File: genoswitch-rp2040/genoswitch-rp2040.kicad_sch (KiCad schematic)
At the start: 35 parts, among them J1 USB_B_Micro, J2 Conn_01x03_Socket-PicoDebug, SW1 BOOTSEL, U1 NCP1117-3.3_SOT223, U2 W25Q128JVS, U3 RP2040, U4 MCP1501-10xCH, U5_HW-SPI0 MCP3008, U6_HW-SPI1 MCP3008, U7_PIO-SPI0 MCP3008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

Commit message: Add 0201/0603M footprints for resistors, capacitors
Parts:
- C1, C10, C101, C11, C12, C13, C14, C15, C16, C4, C5, C6, C7, C8, C9: footprint (none) -> Capacitor_SMD:C_0201_0603Metric
- R1, R2, R3, R4, R5: footprint (none) -> Resistor_SMD:R_0201_0603Metric
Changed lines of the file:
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@@
       (effects (font (size 1.27 1.27)) (justify left))
     )
-    (property "Footprint" "" (at 70.8152 31.75 0)
+    (property "Footprint" "Capacitor_SMD:C_0201_0603Metric" (at 70.8152 31.75 0)
       (effects (font (size 1.27 1.27)) hide)
     )
@@
       (effects (font (size 1.27 1.27)) (justify left))
     )
-    (property "Footprint" "" (at 168.402 25.4 90)
+    (property "Footprint" "Resistor_SMD:R_0201_0603Metric" (at 168.402 25.4 90)
       (effects (font (size 1.27 1.27)) hide)
     )
@@
       (effects (font (size 1.27 1.27)))
     )
-    (property "Footprint" "" (at 354.33 21.8948 0)
+    (property "Footprint" "Capacitor_SMD:C_0201_0603Metric" (at 354.33 21.8948 0)
       (effects (font (size 1.27 1.27)) hide)
     )
@@
       (effects (font (size 1.27 1.27)) (justify left))
     )
-    (property "Footprint" "" (at 168.402 35.56 90)
+    (property "Footprint" "Resistor_SMD:R_0201_0603Metric" (at 168.402 35.56 90)
       (effects (font (size 1.27 1.27)) hide)
     )
@@
       (effects (font (size 1.27 1.27)))
     )
-    (property "Footprint" "" (at 349.25 178.308 90)
+    (property "Footprint" "Resistor_SMD:R_0201_0603Metric" (at 349.25 178.308 90)
       (effects (font (size 1.27 1.27)) hide)
     )
@@
       (effects (font (size 1.27 1.27)) (justify left))
     )
-    (property "Footprint" "" (at 108.9152 31.75 0)
+    (property "Footprint" "Capacitor_SMD:C_0201_0603Metric" (at 108.9152 31.75 0)
       (effects (font (size 1.27 1.27)) hide)
     )
@@
       (effects (font (size 1.27 1.27)) (justify left))
     )
-    (property "Footprint" "" (at 39.0652 31.75 0)
+    (property "Footprint" "Capacitor_SMD:C_0201_0603Metric" (at 39.0652 31.75 0)
       (effects (font (size 1.27 1.27)) hide)
     )
@@
       (effects (font (size 1.27 1.27)))
     )
-    (property "Footprint" "" (at 335.28 35.052 90)
+    (property "Footprint" "Resistor_SMD:R_0201_0603Metric" (at 335.28 35.052 90)
       (effects (font (size 1.27 1.27)) hide)
     )
@@
       (effects (font (size 1.27 1.27)) (justify right))
     )
-    (property "Footprint" "" (at 190.8048 179.07 0)
+    (property "Footprint" "Capacitor_SMD:C_0201_0603Metric" (at 190.8048 179.07 0)
       (effects (font (size 1.27 1.27)) hide)
     )
@@
       (effects (font (size 1.27 1.27)) (justify left))
     )
-    (property "Footprint" "" (at 51.7652 44.45 0)
+    (property "Footprint" "Capacitor_SMD:C_0201_0603Metric" (at 51.7652 44.45 0)
       (effects (font (size 1.27 1.27)) hide)
     )
@@
       (effects (font (size 1.27 1.27)) (justify left))
     )
-    (property "Footprint" "" (at 171.1452 49.53 0)
+    (property "Footprint" "Capacitor_SMD:C_0201_0603Metric" (at 171.1452 49.53 0)
       (effects (font (size 1.27 1.27)) hide)
     )
@@
       (effects (font (size 1.27 1.27)) (justify left))
     )
-    (property "Footprint" "" (at 53.0352 31.75 0)
+    (property "Footprint" "Capacitor_SMD:C_0201_0603Metric" (at 53.0352 31.75 0)
       (effects (font (size 1.27 1.27)) hide)
     )
@@
       (effects (font (size 1.27 1.27)) (justify left))
     )
-    (property "Footprint" "" (at 398.4752 231.14 0)
+    (property "Footprint" "Capacitor_SMD:C_0201_0603Metric" (at 398.4752 231.14 0)
       (effects (font (size 1.27 1.27)) hide)
     )
@@
       (effects (font (size 1.27 1.27)) (justify left))
     )
-    (property "Footprint" "" (at 107.6452 53.34 0)
+    (property "Footprint" "Capacitor_SMD:C_0201_0603Metric" (at 107.6452 53.34 0)
       (effects (font (size 1.27 1.27)) hide)
     )
@@
       (effects (font (size 1.27 1.27)) (justify left))
     )
-    (property "Footprint" "" (at 121.6152 31.75 0)
+    (property "Footprint" "Capacitor_SMD:C_0201_0603Metric" (at 121.6152 31.75 0)
       (effects (font (size 1.27 1.27)) hide)
     )
@@
       (effects (font (size 1.27 1.27)) (justify left))
     )
-    (property "Footprint" "" (at 96.2152 31.75 0)
+    (property "Footprint" "Capacitor_SMD:C_0201_0603Metric" (at 96.2152 31.75 0)
       (effects (font (size 1.27 1.27)) hide)
     )
@@
       (effects (font (size 1.27 1.27)) (justify left))
     )
-    (property "Footprint" "" (at 83.5152 31.75 0)
+    (property "Footprint" "Capacitor_SMD:C_0201_0603Metric" (at 83.5152 31.75 0)
       (effects (font (size 1.27 1.27)) hide)
     )
@@
       (effects (font (size 1.27 1.27)) (justify left))
     )
-    (property "Footprint" "" (at 329.8952 231.14 0)
+    (property "Footprint" "Capacitor_SMD:C_0201_0603Metric" (at 329.8952 231.14 0)
       (effects (font (size 1.27 1.27)) hide)
     )
@@
       (effects (font (size 1.27 1.27)) (justify right))
     )
-    (property "Footprint" "" (at 351.028 31.75 90)
+    (property "Footprint" "Resistor_SMD:R_0201_0603Metric" (at 351.028 31.75 90)
       (effects (font (size 1.27 1.27)) hide)
     )
@@
       (effects (font (size 1.27 1.27)) (justify left))
     )
-    (property "Footprint" "" (at 134.3152 31.75 0)
-      (effects (font (size 1.27 1.27)) hide)
-    )
+    (property "Footprint" "Capacitor_SMD:C_0201_0603Metric" (at 134.3152 31.75 0)
+      (effects (font (size 1.27 1.27)) hide)
+    )

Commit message: Add footprint for Micro-USB 10118193-0001LF
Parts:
- J1: footprint (none) -> Connector_USB:USB_Micro-B_Amphenol_10118193-0001LF_Horizontal
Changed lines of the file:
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@@
       (effects (font (size 1.27 1.27)))
     )
-    (property "Footprint" "" (at 309.88 228.6 0)
+    (property "Footprint" "Connector_USB:USB_Micro-B_Amphenol_10118193-0001LF_Horizontal" (at 309.88 228.6 0)
       (effects (font (size 1.27 1.27)) hide)
     )

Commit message: Add footprint for C2, C3
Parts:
- C2, C3: footprint (none) -> Capacitor_SMD:C_0201_0603Metric
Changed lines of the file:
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@@
       (effects (font (size 1.27 1.27)))
     )
-    (property "Footprint" "" (at 325.12 175.5648 0)
+    (property "Footprint" "Capacitor_SMD:C_0201_0603Metric" (at 325.12 175.5648 0)
       (effects (font (size 1.27 1.27)) hide)
     )
@@
       (effects (font (size 1.27 1.27)))
     )
-    (property "Footprint" "" (at 325.12 165.4048 0)
-      (effects (font (size 1.27 1.27)) hide)
-    )
+    (property "Footprint" "Capacitor_SMD:C_0201_0603Metric" (at 325.12 165.4048 0)
+      (effects (font (size 1.27 1.27)) hide)
+    )

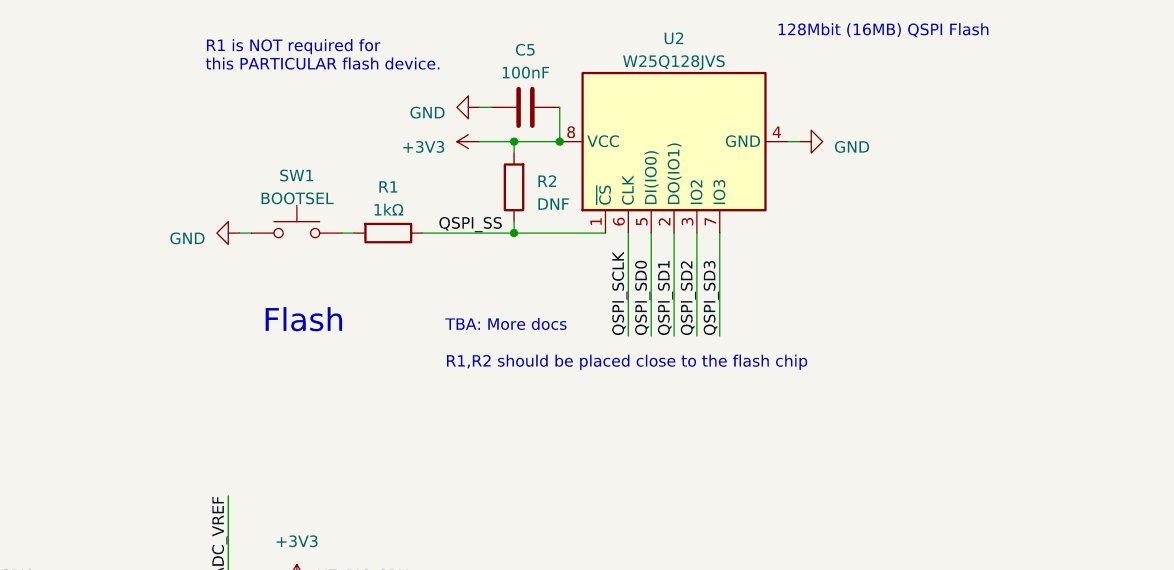
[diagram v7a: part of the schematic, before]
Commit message: Switch SW1 to PTS815 SJM 250 SMTR LFS; add part library
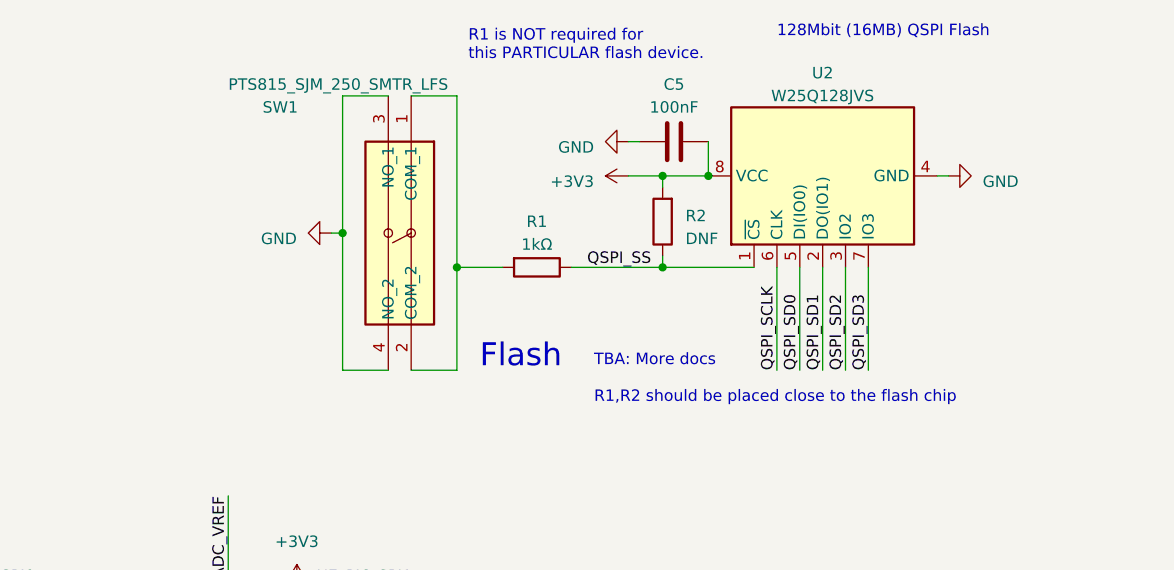
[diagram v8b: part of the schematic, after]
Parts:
- removed SW1: BOOTSEL, symbol Switch:SW_Push
- added SW1: PTS815_SJM_250_SMTR_LFS, PTS815_SJM_250_SMTR_LFS:PTS815SJM250SMTRLFS, symbol PTS815_SJM_250_SMTR_LFS:PTS815_SJM_250_SMTR_LFS
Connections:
- net GND: now also SW1.3 (NO_1), SW1.4 (NO_2)
- net at R1.2: now also SW1.1 (COM_1), SW1.2 (COM_2)
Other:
- moved on the sheet: C5, R1, R2, U2
